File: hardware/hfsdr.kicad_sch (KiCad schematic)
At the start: 57 parts, among them J1 USB_C_Receptacle_USB2.0_16P, SW1 RST, SW2 BOOT0, SW4 RotaryEncoder_Switch, U3 CH32V30xRxTx

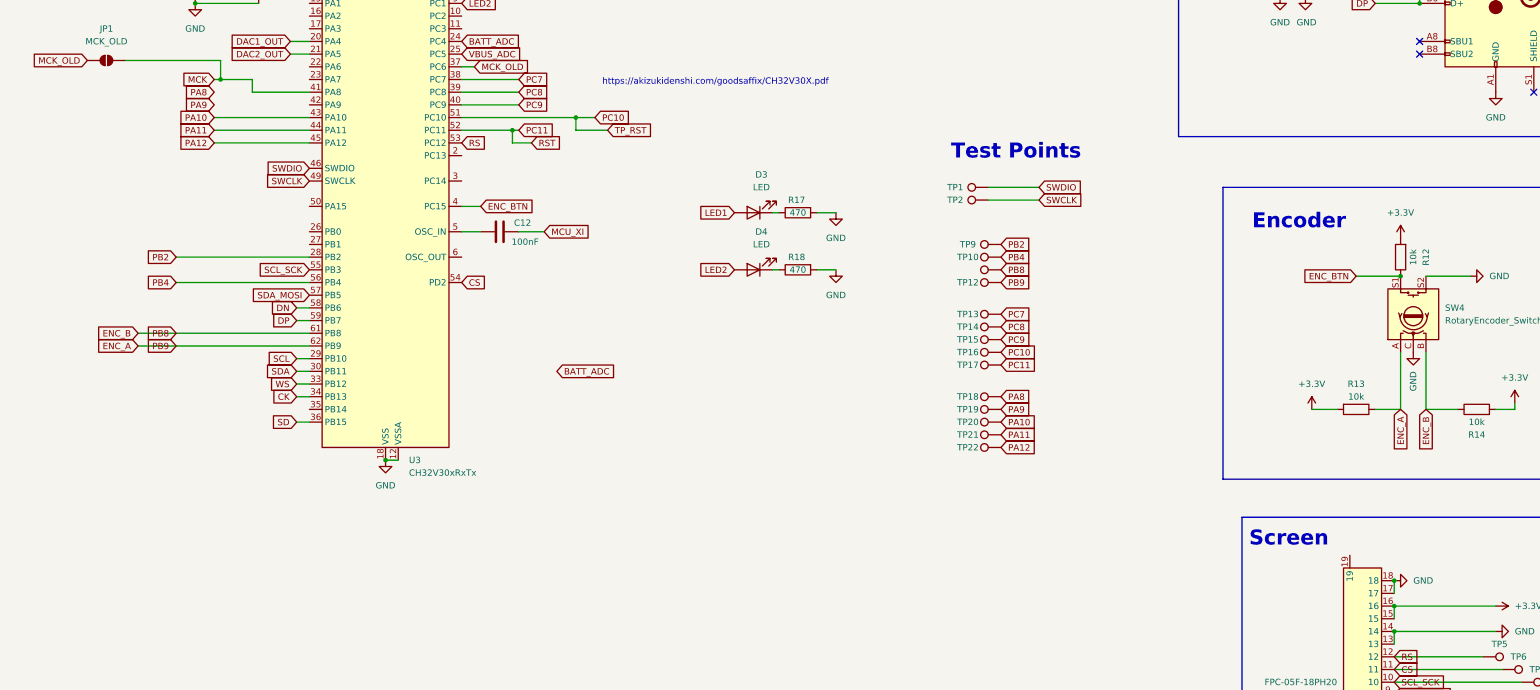
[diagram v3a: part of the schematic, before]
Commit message: hardware: LEDK to TIM3
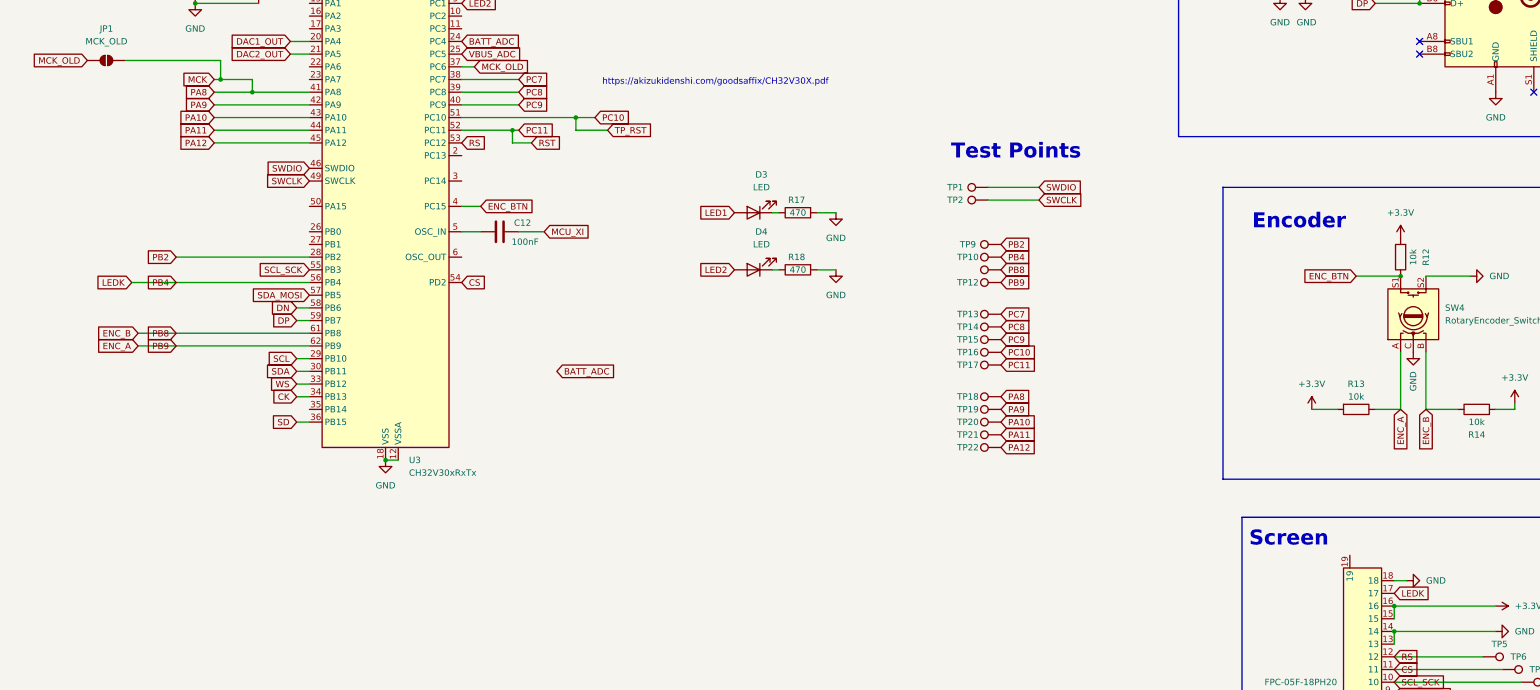
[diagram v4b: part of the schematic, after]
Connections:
- net PA8 is gone; now on net MCK: TP18.1
- net GND: no longer FPC1.17
- net PA9: now also U3.42 (PA9)
- net PB4 renamed LEDK
- net LEDK: now also FPC1.17
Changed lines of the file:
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@@
 	)
 	(junction
-		(at 158.75 46.99)
+		(at 127 87.63)
 		(diameter 0)
 		(color 0 0 0 0)
 	)
 	(junction
-		(at 360.68 69.85)
+		(at 158.75 46.99)
 		(diameter 0)
 		(color 0 0 0 0)
 	)
 	(junction
-		(at 355.6 185.42)
+		(at 360.68 69.85)
 		(diameter 0)
 		(color 0 0 0 0)
@@
 	(wire
 		(pts
-			(xy 355.6 185.42) (xy 355.6 187.96)
+			(xy 172.72 110.49) (xy 168.91 110.49)
 		)
 		(stroke
@@
 	(wire
 		(pts
-			(xy 172.72 110.49) (xy 168.91 110.49)
+			(xy 120.65 81.28) (xy 120.65 85.09)
 		)
 		(stroke
@@
 	(wire
 		(pts
-			(xy 120.65 81.28) (xy 120.65 85.09)
+			(xy 158.75 46.99) (xy 158.75 49.53)
 		)
 		(stroke
@@
 	(wire
 		(pts
-			(xy 158.75 46.99) (xy 158.75 49.53)
+			(xy 119.38 87.63) (xy 127 87.63)
 		)
 		(stroke
@@
 	(wire
 		(pts
+			(xy 102.87 125.73) (xy 138.43 125.73)
+		)
+		(stroke
+			(width 0)
+			(type default)
+		)
+	)
+	(wire
+		(pts
 			(xy 151.13 34.29) (xy 158.75 34.29)
 		)
@@
 	(wire
 		(pts
-			(xy 111.76 125.73) (xy 138.43 125.73)
+			(xy 375.92 151.13) (xy 379.73 151.13)
 		)
 		(stroke
@@
 	(wire
 		(pts
-			(xy 375.92 151.13) (xy 379.73 151.13)
+			(xy 198.12 95.25) (xy 191.77 95.25)
 		)
 		(stroke
@@
 	(wire
 		(pts
-			(xy 198.12 95.25) (xy 191.77 95.25)
+			(xy 191.77 92.71) (xy 168.91 92.71)
 		)
 		(stroke
@@
 	(wire
 		(pts
-			(xy 191.77 92.71) (xy 168.91 92.71)
+			(xy 248.92 270.51) (xy 261.62 270.51)
 		)
 		(stroke
@@
 	(wire
 		(pts
-			(xy 248.92 270.51) (xy 261.62 270.51)
+			(xy 134.62 77.47) (xy 138.43 77.47)
 		)
 		(stroke
@@
 	(wire
 		(pts
-			(xy 134.62 77.47) (xy 138.43 77.47)
+			(xy 359.41 38.1) (xy 359.41 49.53)
 		)
 		(stroke
@@
 	(wire
 		(pts
-			(xy 359.41 38.1) (xy 359.41 49.53)
+			(xy 119.38 90.17) (xy 138.43 90.17)
 		)
 		(stroke
@@
 	(wire
 		(pts
+			(xy 355.6 185.42) (xy 358.14 185.42)
+		)
+		(stroke
+			(width 0)
+			(type default)
+		)
+	)
+	(wire
+		(pts
 			(xy 337.82 64.77) (xy 337.82 68.58)
 		)
@@
 		)
 	)
+	(global_label "LEDK"
+		(shape input)
+		(at 102.87 125.73 180)
+		(fields_autoplaced yes)
+		(effects
+			(font
+				(size 1.27 1.27)
+			)
+			(justify right)
+		)
+		(property "Intersheetrefs" "${INTERSHEET_REFS}"
+			(at 95.1677 125.73 0)
+			(effects
+				(font
+					(size 1.27 1.27)
+				)
+				(justify right)
+				(hide yes)
+			)
+		)
+	)
 	(global_label "DP"
 		(shape input)
@@
 		)
 	)
+	(global_label "LEDK"
+		(shape input)
+		(at 355.6 187.96 0)
+		(fields_autoplaced yes)
+		(effects
+			(font
+				(size 1.27 1.27)
+			)
+			(justify left)
+		)
+		(property "Intersheetrefs" "${INTERSHEET_REFS}"
+			(at 363.3023 187.96 0)
+			(effects
+				(font
+					(size 1.27 1.27)
+				)
+				(justify left)
+				(hide yes)
+			)
+		)
+	)
 	(global_label "ENC_BTN"
 		(shape input)
@@
 	(symbol
 		(lib_id "power:GND")
-		(at 355.6 185.42 90)
+		(at 358.14 185.42 90)
 		(unit 1)
 		(exclude_from_sim no)
@@
 		(fields_autoplaced yes)
 		(property "Reference" "#PWR061"
-			(at 361.95 185.42 0)
+			(at 364.49 185.42 0)
 			(effects
 				(font
@@
 		)
 		(property "Value" "GND"
-			(at 359.41 185.4199 90)
+			(at 361.95 185.4199 90)
 			(effects
 				(font
@@
 		)
 		(property "Footprint" ""
-			(at 355.6 185.42 0)
+			(at 358.14 185.42 0)
 			(effects
 				(font
@@
 		)
 		(property "Datasheet" ""
-			(at 355.6 185.42 0)
+			(at 358.14 185.42 0)
 			(effects
 				(font
@@
 		)
 		(property "Description" "Power symbol creates a global label with name \"GND\" , ground"
-			(at 355.6 185.42 0)
+			(at 358.14 185.42 0)
 			(effects
 				(font

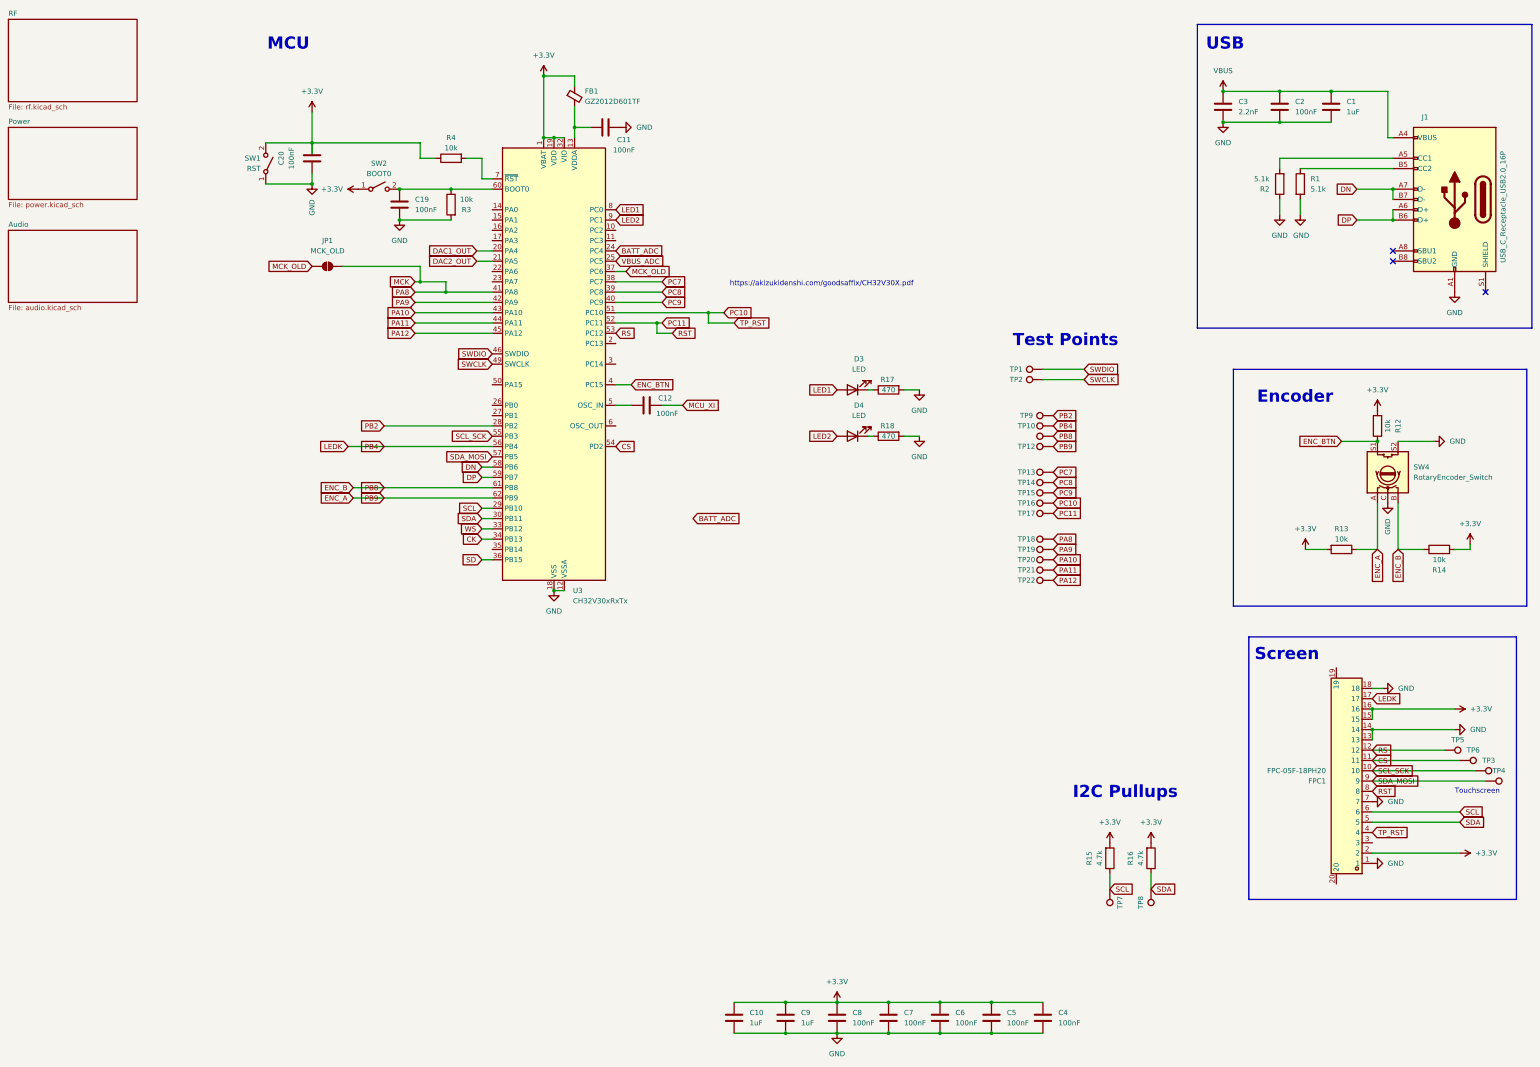
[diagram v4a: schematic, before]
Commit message: hardware feat: interrupt for screen
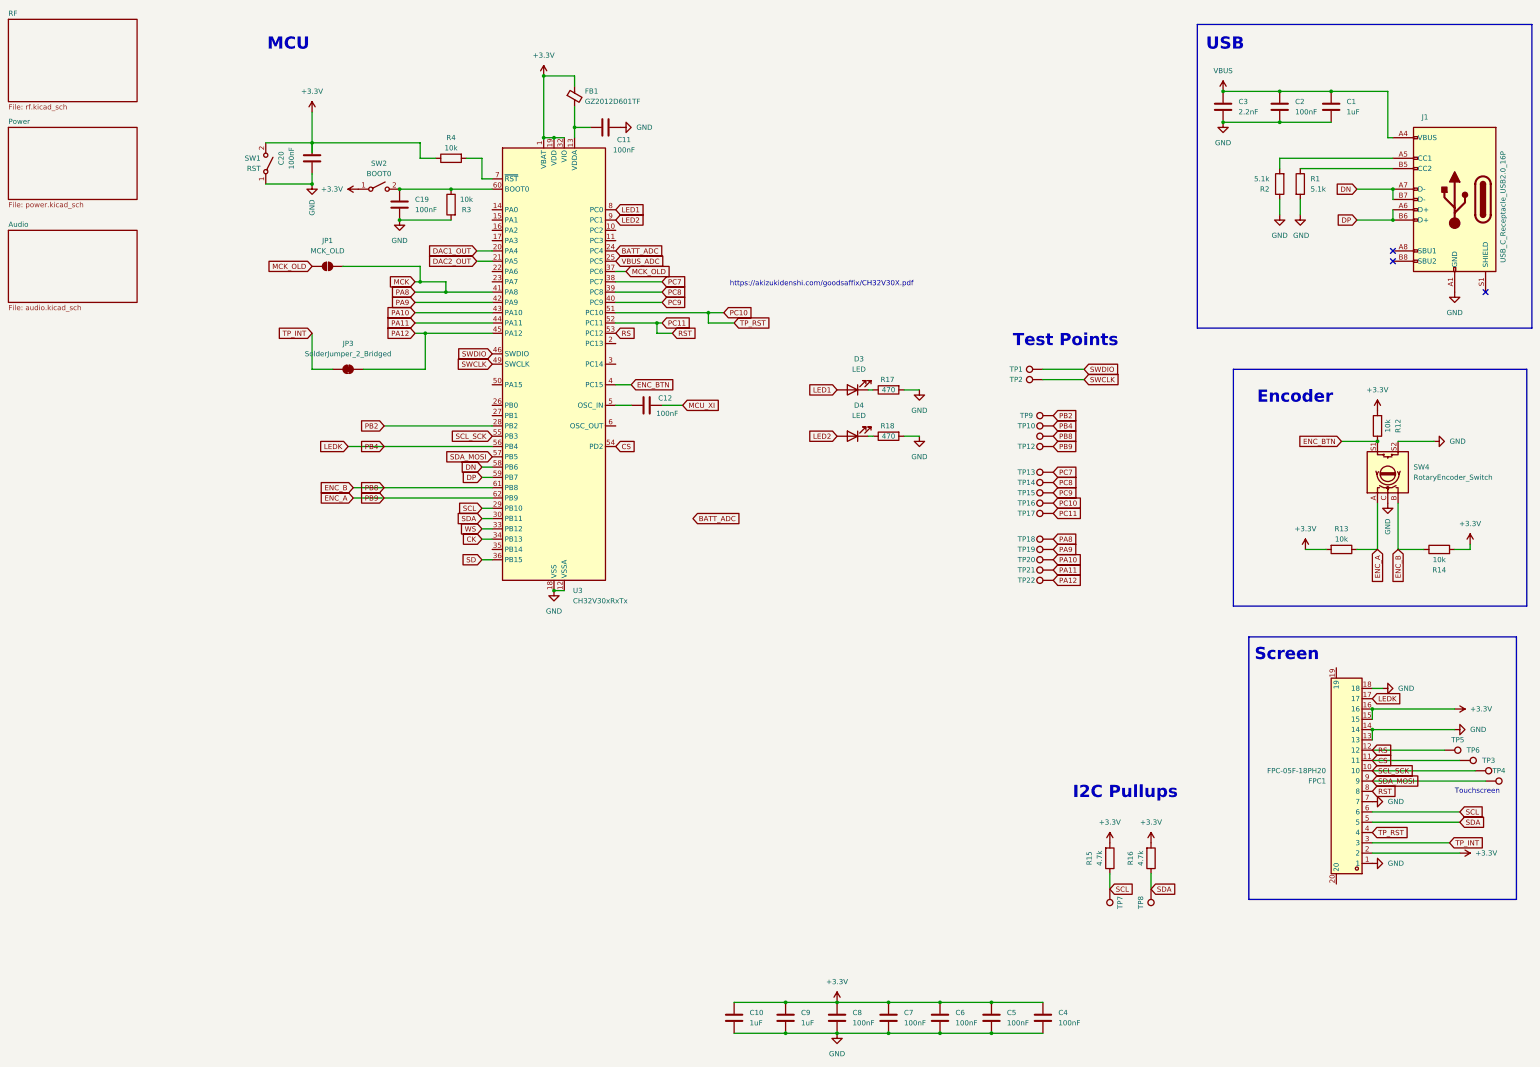
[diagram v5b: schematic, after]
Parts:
- added JP3: SolderJumper_2_Bridged, Jumper:SolderJumper-2_P1.3mm_Bridged2Bar_RoundedPad1.0x1.5mm, symbol Jumper:SolderJumper_2_Bridged
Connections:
- net PA12: now also JP3.2 (B)
- net TP_INT: now reaches FPC1.3
- net TP_INT: now also JP3.1 (A)

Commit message: feat: added tf slot, but need to reroute some screen pins
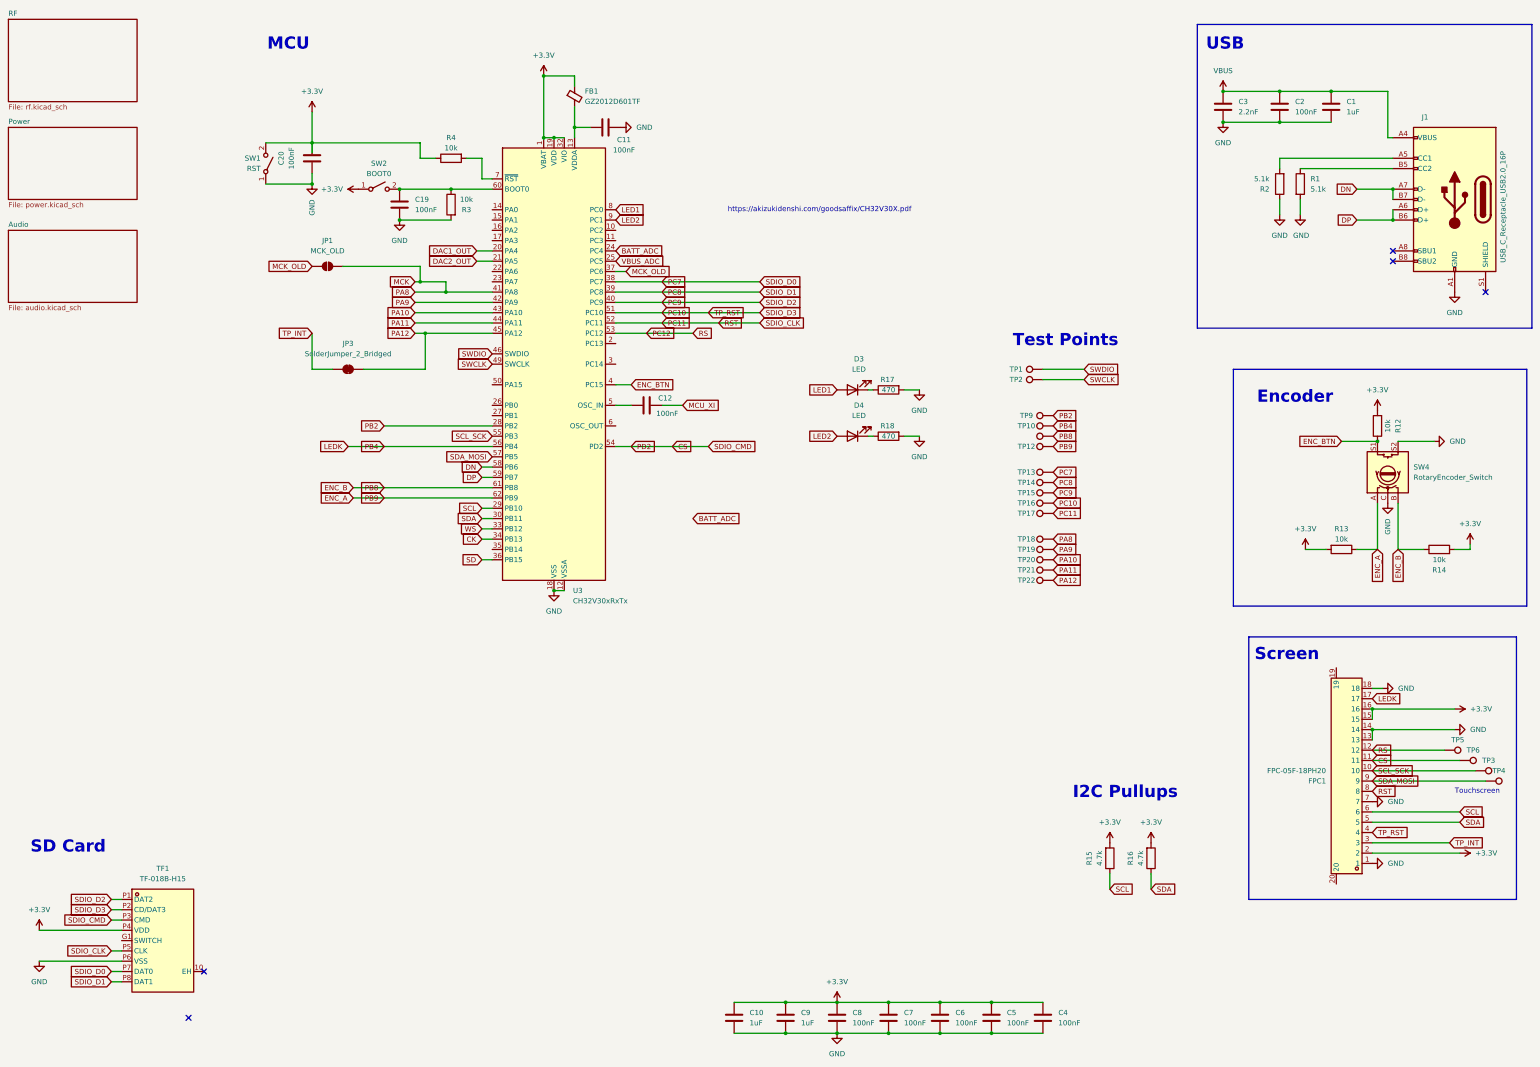
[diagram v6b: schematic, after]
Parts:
- removed TP7, TP8: TestPoint, TestPoint:TestPoint_Pad_1.0x1.0mm, symbol Connector:TestPoint
- added TF1: TF-018B-H15, easyeda:TF-SMD_TF-018B-H15, symbol easyeda:TF-018B-H15
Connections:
- net +3.3V: now also TF1.P4 (VDD)
- net CS: now also TF1.P3 (CMD)
- net GND: now also TF1.P6 (VSS)
- net PC10: now also TF1.P2 (CD/DAT3)
- net PC11: now also TF1.P5 (CLK)
- net PC7: now also TF1.P7 (DAT0)
- net PC8: now also TF1.P8 (DAT1)
- net PC9: now also TF1.P1 (DAT2)
- net RS renamed PC12
- no-connect marks 3 -> 5
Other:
- note added: "SD Card"
